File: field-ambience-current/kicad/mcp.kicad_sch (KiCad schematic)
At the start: 73 parts, among them SW1 Cell 1 digital trigger (HX B3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, SW10 Modifier CLEAR (HX B3F-4055 T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, SW2 Cell 2 digital trigger (HX B3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, SW3 Cell 3 digital trigger (HX B3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, SW4 Cell 4 digital trigger (HX B3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, SW5 Cell 5 digital trigger (HX B3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, SW6 Modifier SHIFT (HX B3F-4055 T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, SW7 Modifier HOLD (HX B3F-4055 TH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, SW8 Modifier DRONE (HX B3F-4055 T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, SW9 Modifier GENERATE (HX B3F-405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, U10 PCA9685PW #2 (16-Ch I²C PWM, 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, U2 MCP23017-E/SS (I/O-Expander), U6 PCA9685PW (16-Ch I²C PWM LED-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

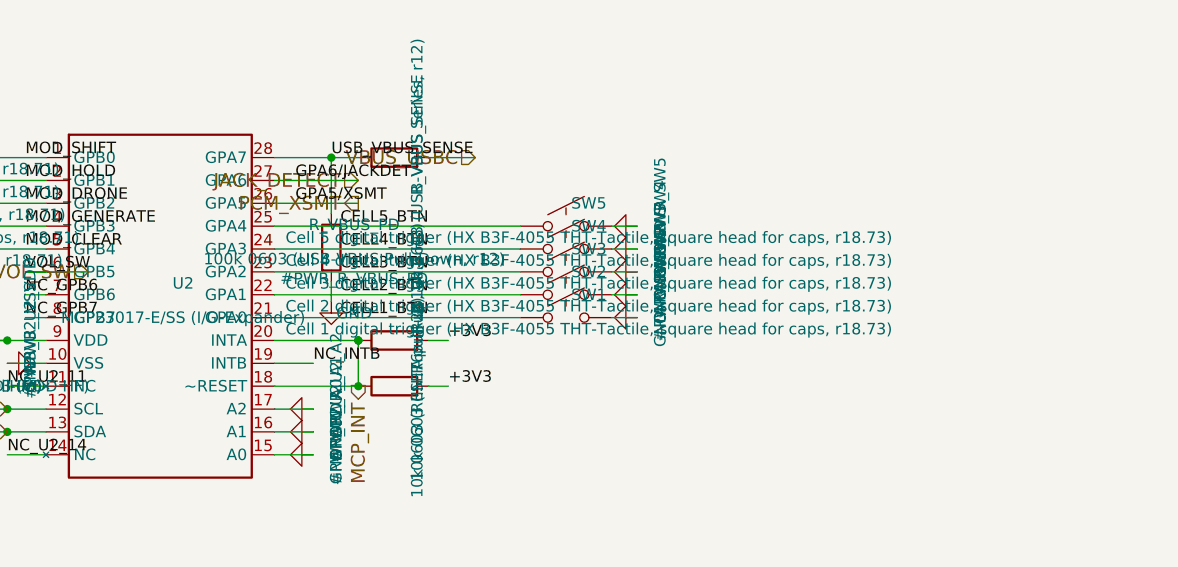
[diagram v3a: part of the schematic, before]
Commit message: cells: real Kailh Choc keyswitch instead of modifier tactile (UX fix, r18.74) (#86)
r18.73 made the 5 cells digital on the MCP23017 but put them on the exact
same small HX B3F-4055 tactile button as the 5 modifier buttons. User feedback:
this makes the playable cells feel identical to a plain modifier button and
kills the "these are keyboard keys" UX that the whole project is built around.

Fix: cells stay electrically digital (identical nets/pins/pull-up/IRQ on
MCP23017 GPA0-GPA4 as r18.73), but now use a Kailh Choc V1/V2 hot-swap socket
instead — the real Kailh Choc keyswitch (~3mm genuine travel) clicks into it
from the front, no soldering of the switch itself, swappable if one dies.
This is exactly the "Plain Choc V2" option already listed in ADR-0013's own
comparison table, just without the Hall/velocity part.

Footprint: Switch_Keyboard_Hotswap_Kailh:SW_Hotswap_Kailh_Choc_V1V2_Plated_1.00u
- already vendored in this repo (MIT-licensed keyswitch-kicad-library),
already registered in fp-lib-table. Community-verified, widely used in shipped
mechanical-keyboard PCBs, but not independently re-checked by this project
against Kailh's own mechanical drawing.

Sourcing, verified vs guessed:
- The hot-swap socket itself has no clean manufacturer/LCSC part number
  anywhere - flagged UNVERIFIED - NEEDS HUMAN CHECK rather than invented.
  It's a keyboard-market item (e.g. Chosfox ~$1.45/10pcs), same sourcing
  category the original Gateron switches were in.
- The switch that clicks in has one confirmed real example: Kailh CPG135001D01
  (red/linear), LCSC C400229, with a real datasheet. Feel/color/V1-vs-V2 is
  an industrial-design choice, not a schematic decision.

Modifier buttons SW6-SW10 are unchanged (still HX B3F-4055 THT tactile) -
this is the deliberate UX split: cells feel like keyboard keys, modifiers
feel like plain buttons.

Regenerated schematics, jlc_bom.csv, and Aron's bom_overview.html. Synced
BOM_MASTER §7, PCB_BOM, PINMAP, KICAD_BLUEPRINT, SCHEMATIC_WALK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
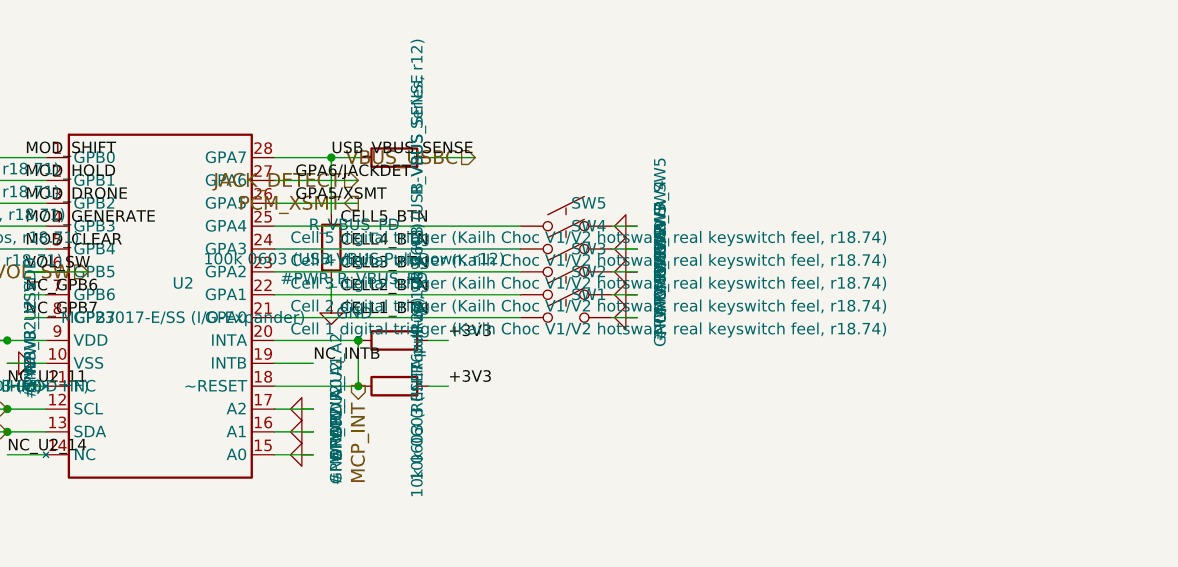
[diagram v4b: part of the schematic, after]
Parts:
- SW1: value Cell 1 digital trigger (HX B3F-4055 THT-Tactile, square head for caps, r18.73) -> Cell 1 digital trigger (Kailh Choc V1/V2 hotswap, real keyswitch feel, r18.74); footprint field_ambience:SW_TC1212-7.3_THT_4P -> Switch_Keyboard_Hotswap_Kailh:SW_Hotswap_Kailh_Choc_V1V2_Plated_1.00u; FP_NOTE r18.73: Cell digital-switch (ADR-0013 superseded). Same ver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 -> Footprint Switch_Keyboard_Hotswap_Kailh:SW_Hotswap_Kailh_Ch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; LCSC C36498965 -> (none); LCSC (switch example, verified in-stock) (none) -> C400229 (CPG135001D01, Choc V1 red/linear) -- other Choc V1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; MPN HX B3F-4055-Y -> Kailh Choc V1 (CPG1350-series) / V2 (CPG1353-series) -- soc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; Manufacturer HX -> Kailh (Dongguan Kaihua Electronics); Package THT 4-pin 11.8x11.8mm, square-head plunger 7.3mm (clip-on c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 -> Hotswap: switch NOT soldered, clicks into an SMD socket on 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; SOCKET-SOURCING (none) -> UNVERIFIED -- NEEDS HUMAN CHECK: the hotswap socket clip it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; STEM-NOTE (none) -> Choc V1 and V2 use different keycap stems (V1 proprietary b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
- SW2: value Cell 2 digital trigger (HX B3F-4055 THT-Tactile, square head for caps, r18.73) -> Cell 2 digital trigger (Kailh Choc V1/V2 hotswap, real keyswitch feel, r18.74); footprint field_ambience:SW_TC1212-7.3_THT_4P -> Switch_Keyboard_Hotswap_Kailh:SW_Hotswap_Kailh_Choc_V1V2_Plated_1.00u; FP_NOTE r18.73: Cell digital-switch (ADR-0013 superseded). Same ver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 -> Footprint Switch_Keyboard_Hotswap_Kailh:SW_Hotswap_Kailh_Ch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; LCSC C36498965 -> (none); LCSC (switch example, verified in-stock) (none) -> C400229 (CPG135001D01, Choc V1 red/linear) -- other Choc V1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; MPN HX B3F-4055-Y -> Kailh Choc V1 (CPG1350-series) / V2 (CPG1353-series) -- soc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; Manufacturer HX -> Kailh (Dongguan Kaihua Electronics); Package THT 4-pin 11.8x11.8mm, square-head plunger 7.3mm (clip-on c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 -> Hotswap: switch NOT soldered, clicks into an SMD socket on 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; SOCKET-SOURCING (none) -> UNVERIFIED -- NEEDS HUMAN CHECK: the hotswap socket clip it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; STEM-NOTE (none) -> Choc V1 and V2 use different keycap stems (V1 proprietary b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
- SW3: value Cell 3 digital trigger (HX B3F-4055 THT-Tactile, square head for caps, r18.73) -> Cell 3 digital trigger (Kailh Choc V1/V2 hotswap, real keyswitch feel, r18.74); footprint field_ambience:SW_TC1212-7.3_THT_4P -> Switch_Keyboard_Hotswap_Kailh:SW_Hotswap_Kailh_Choc_V1V2_Plated_1.00u; FP_NOTE r18.73: Cell digital-switch (ADR-0013 superseded). Same ver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 -> Footprint Switch_Keyboard_Hotswap_Kailh:SW_Hotswap_Kailh_Ch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; LCSC C36498965 -> (none); LCSC (switch example, verified in-stock) (none) -> C400229 (CPG135001D01, Choc V1 red/linear) -- other Choc V1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; MPN HX B3F-4055-Y -> Kailh Choc V1 (CPG1350-series) / V2 (CPG1353-series) -- soc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; Manufacturer HX -> Kailh (Dongguan Kaihua Electronics); Package THT 4-pin 11.8x11.8mm, square-head plunger 7.3mm (clip-on c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 -> Hotswap: switch NOT soldered, clicks into an SMD socket on 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; SOCKET-SOURCING (none) -> UNVERIFIED -- NEEDS HUMAN CHECK: the hotswap socket clip it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; STEM-NOTE (none) -> Choc V1 and V2 use different keycap stems (V1 proprietary b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
- SW4: value Cell 4 digital trigger (HX B3F-4055 THT-Tactile, square head for caps, r18.73) -> Cell 4 digital trigger (Kailh Choc V1/V2 hotswap, real keyswitch feel, r18.74); footprint field_ambience:SW_TC1212-7.3_THT_4P -> Switch_Keyboard_Hotswap_Kailh:SW_Hotswap_Kailh_Choc_V1V2_Plated_1.00u; FP_NOTE r18.73: Cell digital-switch (ADR-0013 superseded). Same ver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 -> Footprint Switch_Keyboard_Hotswap_Kailh:SW_Hotswap_Kailh_Ch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; LCSC C36498965 -> (none); LCSC (switch example, verified in-stock) (none) -> C400229 (CPG135001D01, Choc V1 red/linear) -- other Choc V1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; MPN HX B3F-4055-Y -> Kailh Choc V1 (CPG1350-series) / V2 (CPG1353-series) -- soc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; Manufacturer HX -> Kailh (Dongguan Kaihua Electronics); Package THT 4-pin 11.8x11.8mm, square-head plunger 7.3mm (clip-on c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 -> Hotswap: switch NOT soldered, clicks into an SMD socket on 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; SOCKET-SOURCING (none) -> UNVERIFIED -- NEEDS HUMAN CHECK: the hotswap socket clip it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; STEM-NOTE (none) -> Choc V1 and V2 use different keycap stems (V1 proprietary b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
- SW5: value Cell 5 digital trigger (HX B3F-4055 THT-Tactile, square head for caps, r18.73) -> Cell 5 digital trigger (Kailh Choc V1/V2 hotswap, real keyswitch feel, r18.74); footprint field_ambience:SW_TC1212-7.3_THT_4P -> Switch_Keyboard_Hotswap_Kailh:SW_Hotswap_Kailh_Choc_V1V2_Plated_1.00u; FP_NOTE r18.73: Cell digital-switch (ADR-0013 superseded). Same ver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 -> Footprint Switch_Keyboard_Hotswap_Kailh:SW_Hotswap_Kailh_Ch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; LCSC C36498965 -> (none); LCSC (switch example, verified in-stock) (none) -> C400229 (CPG135001D01, Choc V1 red/linear) -- other Choc V1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; MPN HX B3F-4055-Y -> Kailh Choc V1 (CPG1350-series) / V2 (CPG1353-series) -- soc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; Manufacturer HX -> Kailh (Dongguan Kaihua Electronics); Package THT 4-pin 11.8x11.8mm, square-head plunger 7.3mm (clip-on c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 -> Hotswap: switch NOT soldered, clicks into an SMD socket on 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; SOCKET-SOURCING (none) -> UNVERIFIED -- NEEDS HUMAN CHECK: the hotswap socket clip it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; STEM-NOTE (none) -> Choc V1 and V2 use different keycap stems (V1 proprietary b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

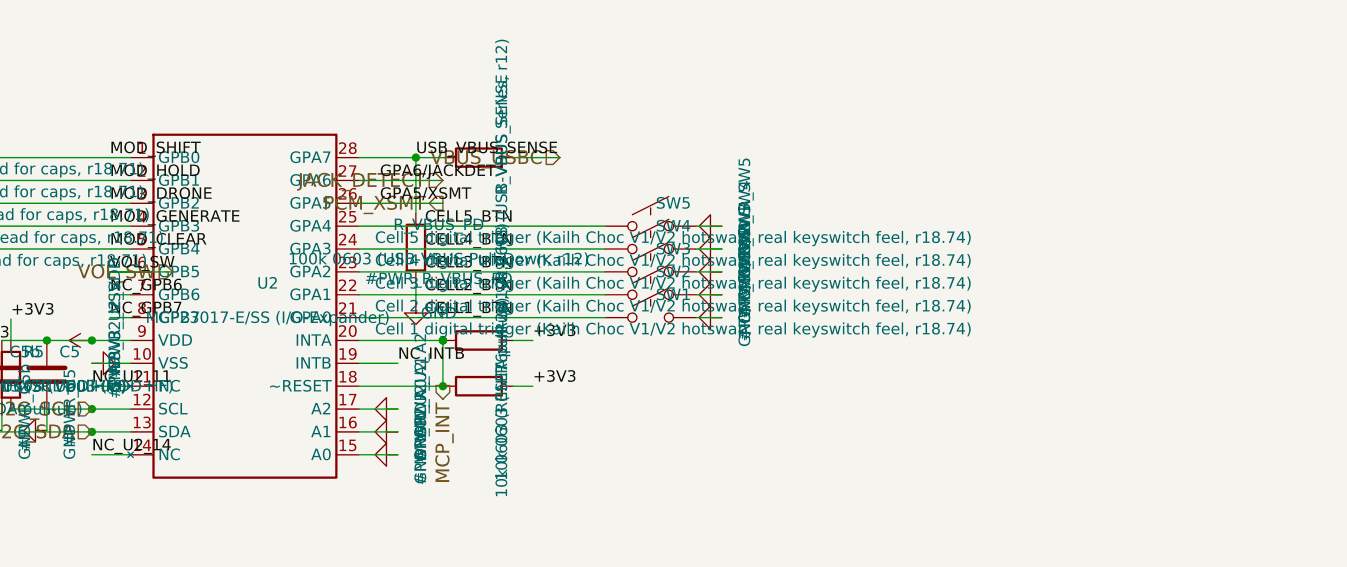
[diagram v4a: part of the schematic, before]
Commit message: cells: direct-solder Kailh Choc V1 instead of hot-swap socket (r18.75) (#87)
User feedback on the r18.74 hot-swap-socket plan: "This is wrong. How is
this meant to be soldered onto a pcb? ... maybe we can just directly solder
the kalih choc on the pcb?"

Fair concern: the r18.74 hot-swap socket had no clean manufacturer/LCSC part
number, and would have needed a non-obvious small-SMD hand-soldering
technique (2 tiny SMD pads on the back, switch clicks in separately from the
front) that isn't obvious without prior hobbyist-keyboard experience.

Fix: the Kailh Choc V1 switch (CPG135001D01) is now directly soldered to the
board -- 2 THT legs through 2 holes, soldered from the back, exactly the
same technique as every other button/connector in this design. No hot-swap
socket, no special technique. Trade-off: the switch is now permanent (not
swappable without desoldering) -- worth it for assembly simplicity and
dropping an unverified part.

Footprint + 3D STEP pulled directly from LCSC/EasyEDA for this exact part:
easyeda2kicad --full --lcsc_id=C400229 -- this repo's own documented method
for custom footprints (same as TS-1088, MST-12D18, PJ-320D), not a
third-party keyboard library. Vendored as
field_ambience:SW_KailhChoc_CPG1350_THT_2P with a real 3D STEP model.

Verified facts, nothing guessed:
- CPG135001D01 / LCSC C400229 is a real, confirmed listing with a real
  datasheet (red/linear Choc V1).
- JLCPCB's own page notes their automated PCBA line needs a custom assembly
  fixture for this THT part, and shows 0 stock at time of writing -- neither
  blocks hand-soldering it yourself, which needs no fixture.
- The footprint pulled from LCSC/EasyEDA has 2 electrical THT pads + 3
  unplated mechanical locator holes matching the switch's own alignment pegs
  (no plate strictly required).

This closes the UNKNOWN classification that r18.74 had opened in
PCB_FOOTPRINT_RISK_AUDIT.md (the hot-swap socket with no clean part number)
-- back to 0 unknowns.

Electrically unchanged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
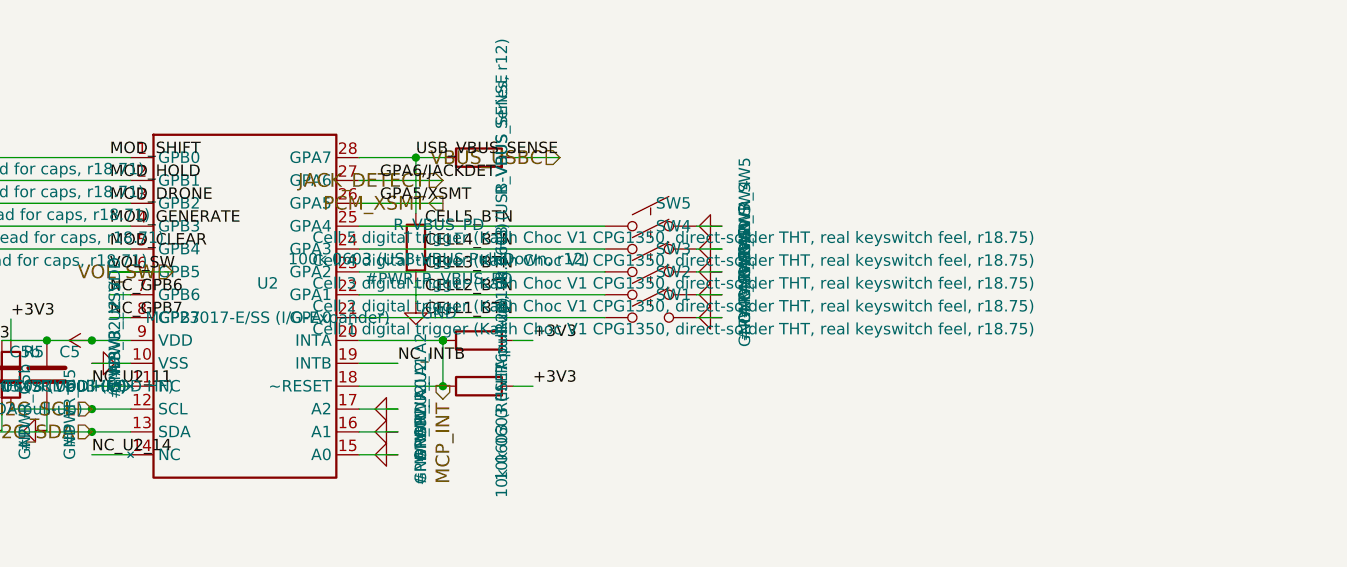
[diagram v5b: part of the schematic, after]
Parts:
- SW1: value Cell 1 digital trigger (Kailh Choc V1/V2 hotswap, real keyswitch feel, r18.74) -> Cell 1 digital trigger (Kailh Choc V1 CPG1350, direct-solder THT, real keyswitch feel, r18.75); footprint Switch_Keyboard_Hotswap_Kailh:SW_Hotswap_Kailh_Choc_V1V2_Plated_1.00u -> field_ambience:SW_KailhChoc_CPG1350_THT_2P; COLOR-NOTE (none) -> Other Choc V1 colors (tactile/clicky) share the same 2-pin 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; FP_NOTE Footprint Switch_Keyboard_Hotswap_Kailh:SW_Hotswap_Kailh_Ch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 -> field_ambience:SW_KailhChoc_CPG1350_THT_2P -- pulled direct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; LCSC (none) -> C400229; LCSC (switch example, verified in-stock) C400229 (CPG135001D01, Choc V1 red/linear) -- other Choc V1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 -> (none); MPN Kailh Choc V1 (CPG1350-series) / V2 (CPG1353-series) -- soc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 -> CPG135001D01 (Kailh Choc V1, red/linear); Package Hotswap: switch NOT soldered, clicks into an SMD socket on 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 -> Direct-solder THT, 2 electrical pins + 3 unplated mechanica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; SOCKET-SOURCING UNVERIFIED -- NEEDS HUMAN CHECK: the hotswap socket clip it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 -> (none); SOURCING-NOTE (none) -> C400229 is a verified real LCSC listing. JLCPCB's own page 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; STEM-NOTE Choc V1 and V2 use different keycap stems (V1 proprietary b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 -> (none); TRADE-OFF (none) -> r18.75 (was r18.74 Kailh-Choc-hotswap-socket): switch is no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
- SW2: value Cell 2 digital trigger (Kailh Choc V1/V2 hotswap, real keyswitch feel, r18.74) -> Cell 2 digital trigger (Kailh Choc V1 CPG1350, direct-solder THT, real keyswitch feel, r18.75); footprint Switch_Keyboard_Hotswap_Kailh:SW_Hotswap_Kailh_Choc_V1V2_Plated_1.00u -> field_ambience:SW_KailhChoc_CPG1350_THT_2P; COLOR-NOTE (none) -> Other Choc V1 colors (tactile/clicky) share the same 2-pin 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; FP_NOTE Footprint Switch_Keyboard_Hotswap_Kailh:SW_Hotswap_Kailh_Ch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 -> field_ambience:SW_KailhChoc_CPG1350_THT_2P -- pulled direct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; LCSC (none) -> C400229; LCSC (switch example, verified in-stock) C400229 (CPG135001D01, Choc V1 red/linear) -- other Choc V1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 -> (none); MPN Kailh Choc V1 (CPG1350-series) / V2 (CPG1353-series) -- soc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 -> CPG135001D01 (Kailh Choc V1, red/linear); Package Hotswap: switch NOT soldered, clicks into an SMD socket on 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 -> Direct-solder THT, 2 electrical pins + 3 unplated mechanica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; SOCKET-SOURCING UNVERIFIED -- NEEDS HUMAN CHECK: the hotswap socket clip it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 -> (none); SOURCING-NOTE (none) -> C400229 is a verified real LCSC listing. JLCPCB's own page 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; STEM-NOTE Choc V1 and V2 use different keycap stems (V1 proprietary b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 -> (none); TRADE-OFF (none) -> r18.75 (was r18.74 Kailh-Choc-hotswap-socket): switch is no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
- SW3: value Cell 3 digital trigger (Kailh Choc V1/V2 hotswap, real keyswitch feel, r18.74) -> Cell 3 digital trigger (Kailh Choc V1 CPG1350, direct-solder THT, real keyswitch feel, r18.75); footprint Switch_Keyboard_Hotswap_Kailh:SW_Hotswap_Kailh_Choc_V1V2_Plated_1.00u -> field_ambience:SW_KailhChoc_CPG1350_THT_2P; COLOR-NOTE (none) -> Other Choc V1 colors (tactile/clicky) share the same 2-pin 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; FP_NOTE Footprint Switch_Keyboard_Hotswap_Kailh:SW_Hotswap_Kailh_Ch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 -> field_ambience:SW_KailhChoc_CPG1350_THT_2P -- pulled direct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; LCSC (none) -> C400229; LCSC (switch example, verified in-stock) C400229 (CPG135001D01, Choc V1 red/linear) -- other Choc V1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 -> (none); MPN Kailh Choc V1 (CPG1350-series) / V2 (CPG1353-series) -- soc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 -> CPG135001D01 (Kailh Choc V1, red/linear); Package Hotswap: switch NOT soldered, clicks into an SMD socket on 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 -> Direct-solder THT, 2 electrical pins + 3 unplated mechanica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; SOCKET-SOURCING UNVERIFIED -- NEEDS HUMAN CHECK: the hotswap socket clip it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 -> (none); SOURCING-NOTE (none) -> C400229 is a verified real LCSC listing. JLCPCB's own page 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; STEM-NOTE Choc V1 and V2 use different keycap stems (V1 proprietary b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 -> (none); TRADE-OFF (none) -> r18.75 (was r18.74 Kailh-Choc-hotswap-socket): switch is no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
- SW4: value Cell 4 digital trigger (Kailh Choc V1/V2 hotswap, real keyswitch feel, r18.74) -> Cell 4 digital trigger (Kailh Choc V1 CPG1350, direct-solder THT, real keyswitch feel, r18.75); footprint Switch_Keyboard_Hotswap_Kailh:SW_Hotswap_Kailh_Choc_V1V2_Plated_1.00u -> field_ambience:SW_KailhChoc_CPG1350_THT_2P; COLOR-NOTE (none) -> Other Choc V1 colors (tactile/clicky) share the same 2-pin 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; FP_NOTE Footprint Switch_Keyboard_Hotswap_Kailh:SW_Hotswap_Kailh_Ch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 -> field_ambience:SW_KailhChoc_CPG1350_THT_2P -- pulled direct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; LCSC (none) -> C400229; LCSC (switch example, verified in-stock) C400229 (CPG135001D01, Choc V1 red/linear) -- other Choc V1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 -> (none); MPN Kailh Choc V1 (CPG1350-series) / V2 (CPG1353-series) -- soc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 -> CPG135001D01 (Kailh Choc V1, red/linear); Package Hotswap: switch NOT soldered, clicks into an SMD socket on 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 -> Direct-solder THT, 2 electrical pins + 3 unplated mechanica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; SOCKET-SOURCING UNVERIFIED -- NEEDS HUMAN CHECK: the hotswap socket clip it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 -> (none); SOURCING-NOTE (none) -> C400229 is a verified real LCSC listing. JLCPCB's own page 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; STEM-NOTE Choc V1 and V2 use different keycap stems (V1 proprietary b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 -> (none); TRADE-OFF (none) -> r18.75 (was r18.74 Kailh-Choc-hotswap-socket): switch is no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
- SW5: value Cell 5 digital trigger (Kailh Choc V1/V2 hotswap, real keyswitch feel, r18.74) -> Cell 5 digital trigger (Kailh Choc V1 CPG1350, direct-solder THT, real keyswitch feel, r18.75); footprint Switch_Keyboard_Hotswap_Kailh:SW_Hotswap_Kailh_Choc_V1V2_Plated_1.00u -> field_ambience:SW_KailhChoc_CPG1350_THT_2P; COLOR-NOTE (none) -> Other Choc V1 colors (tactile/clicky) share the same 2-pin 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; FP_NOTE Footprint Switch_Keyboard_Hotswap_Kailh:SW_Hotswap_Kailh_Ch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 -> field_ambience:SW_KailhChoc_CPG1350_THT_2P -- pulled direct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; LCSC (none) -> C400229; LCSC (switch example, verified in-stock) C400229 (CPG135001D01, Choc V1 red/linear) -- other Choc V1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 -> (none); MPN Kailh Choc V1 (CPG1350-series) / V2 (CPG1353-series) -- soc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 -> CPG135001D01 (Kailh Choc V1, red/linear); Package Hotswap: switch NOT soldered, clicks into an SMD socket on 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 -> Direct-solder THT, 2 electrical pins + 3 unplated mechanica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; SOCKET-SOURCING UNVERIFIED -- NEEDS HUMAN CHECK: the hotswap socket clip it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 -> (none); SOURCING-NOTE (none) -> C400229 is a verified real LCSC listing. JLCPCB's own page 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; STEM-NOTE Choc V1 and V2 use different keycap stems (V1 proprietary b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 -> (none); TRADE-OFF (none) -> r18.75 (was r18.74 Kailh-Choc-hotswap-socket): switch is no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
